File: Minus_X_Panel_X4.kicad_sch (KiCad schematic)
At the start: 9 parts

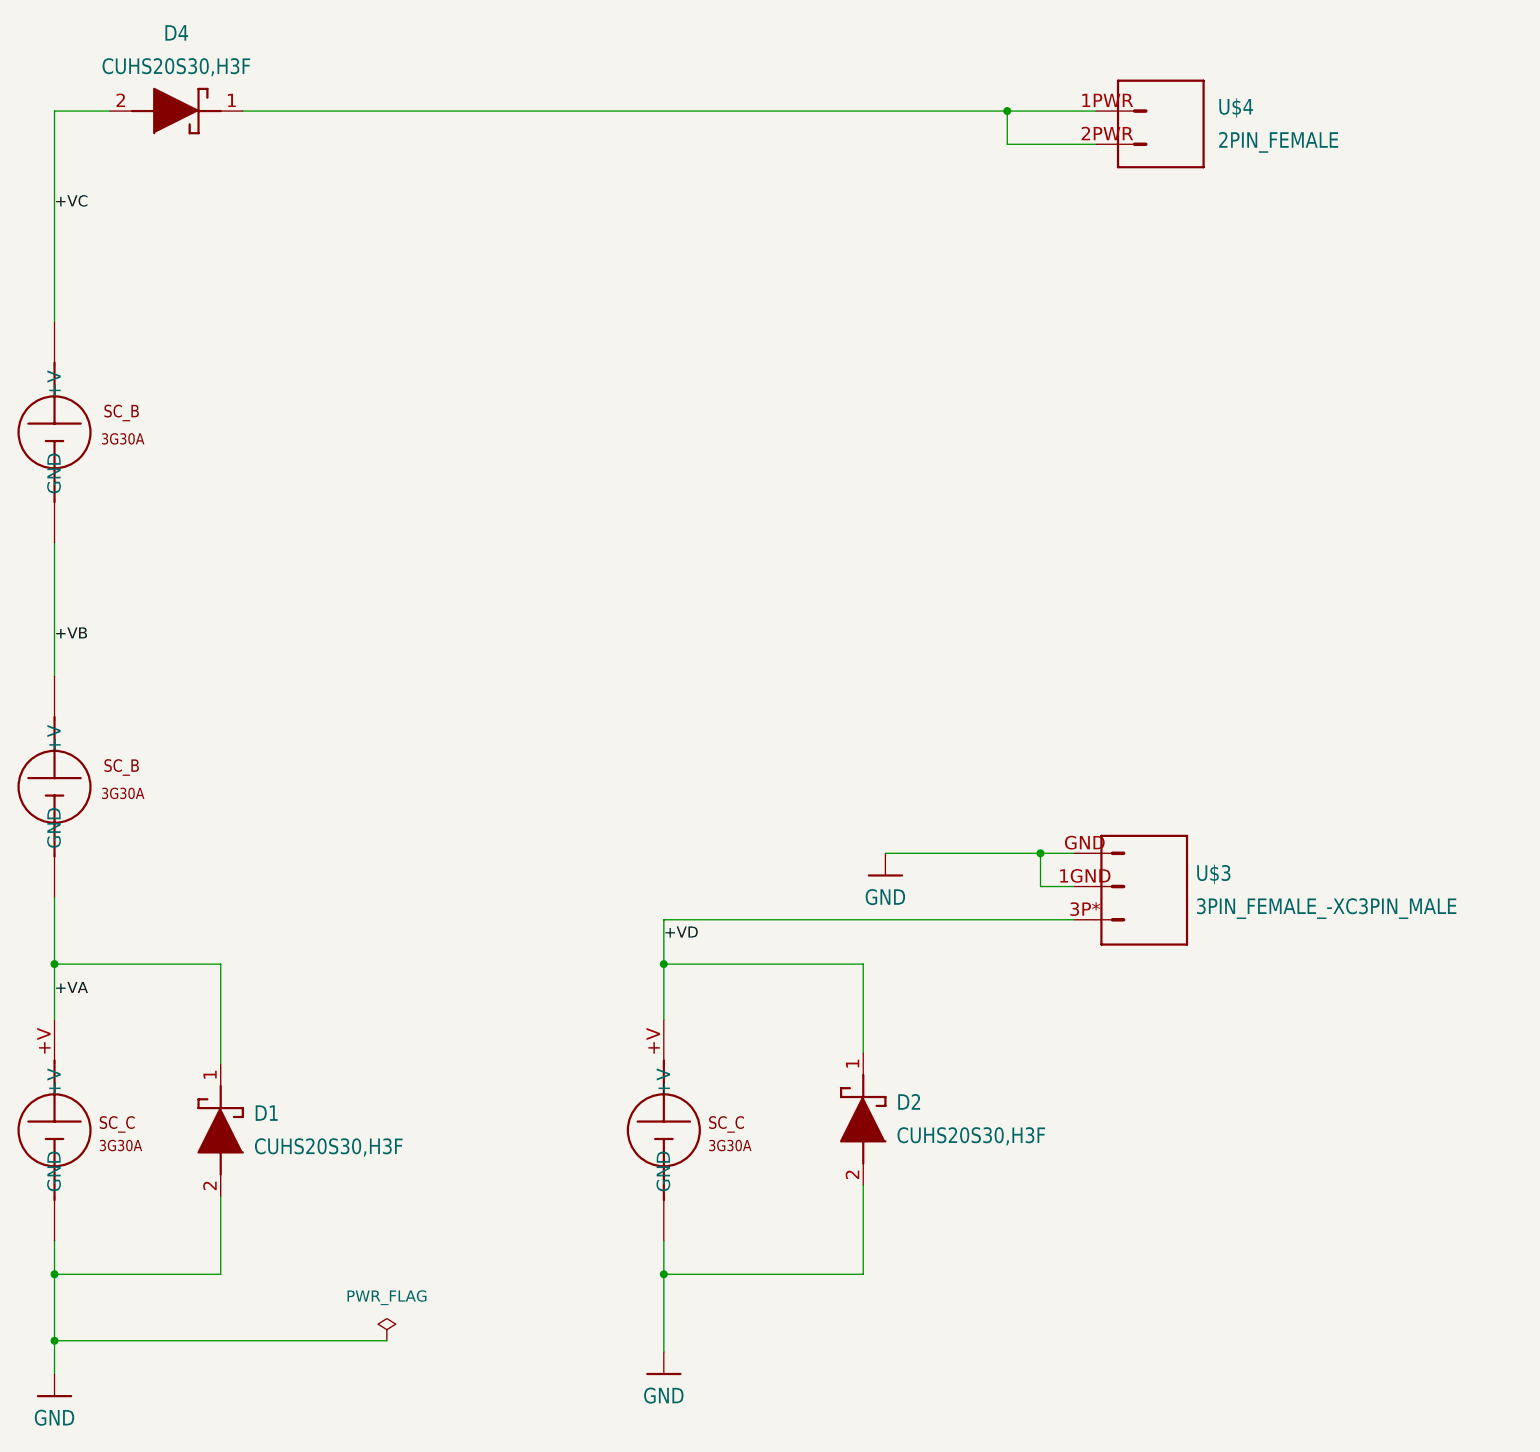
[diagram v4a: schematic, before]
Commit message: footprint of the Panel is modified with tracking
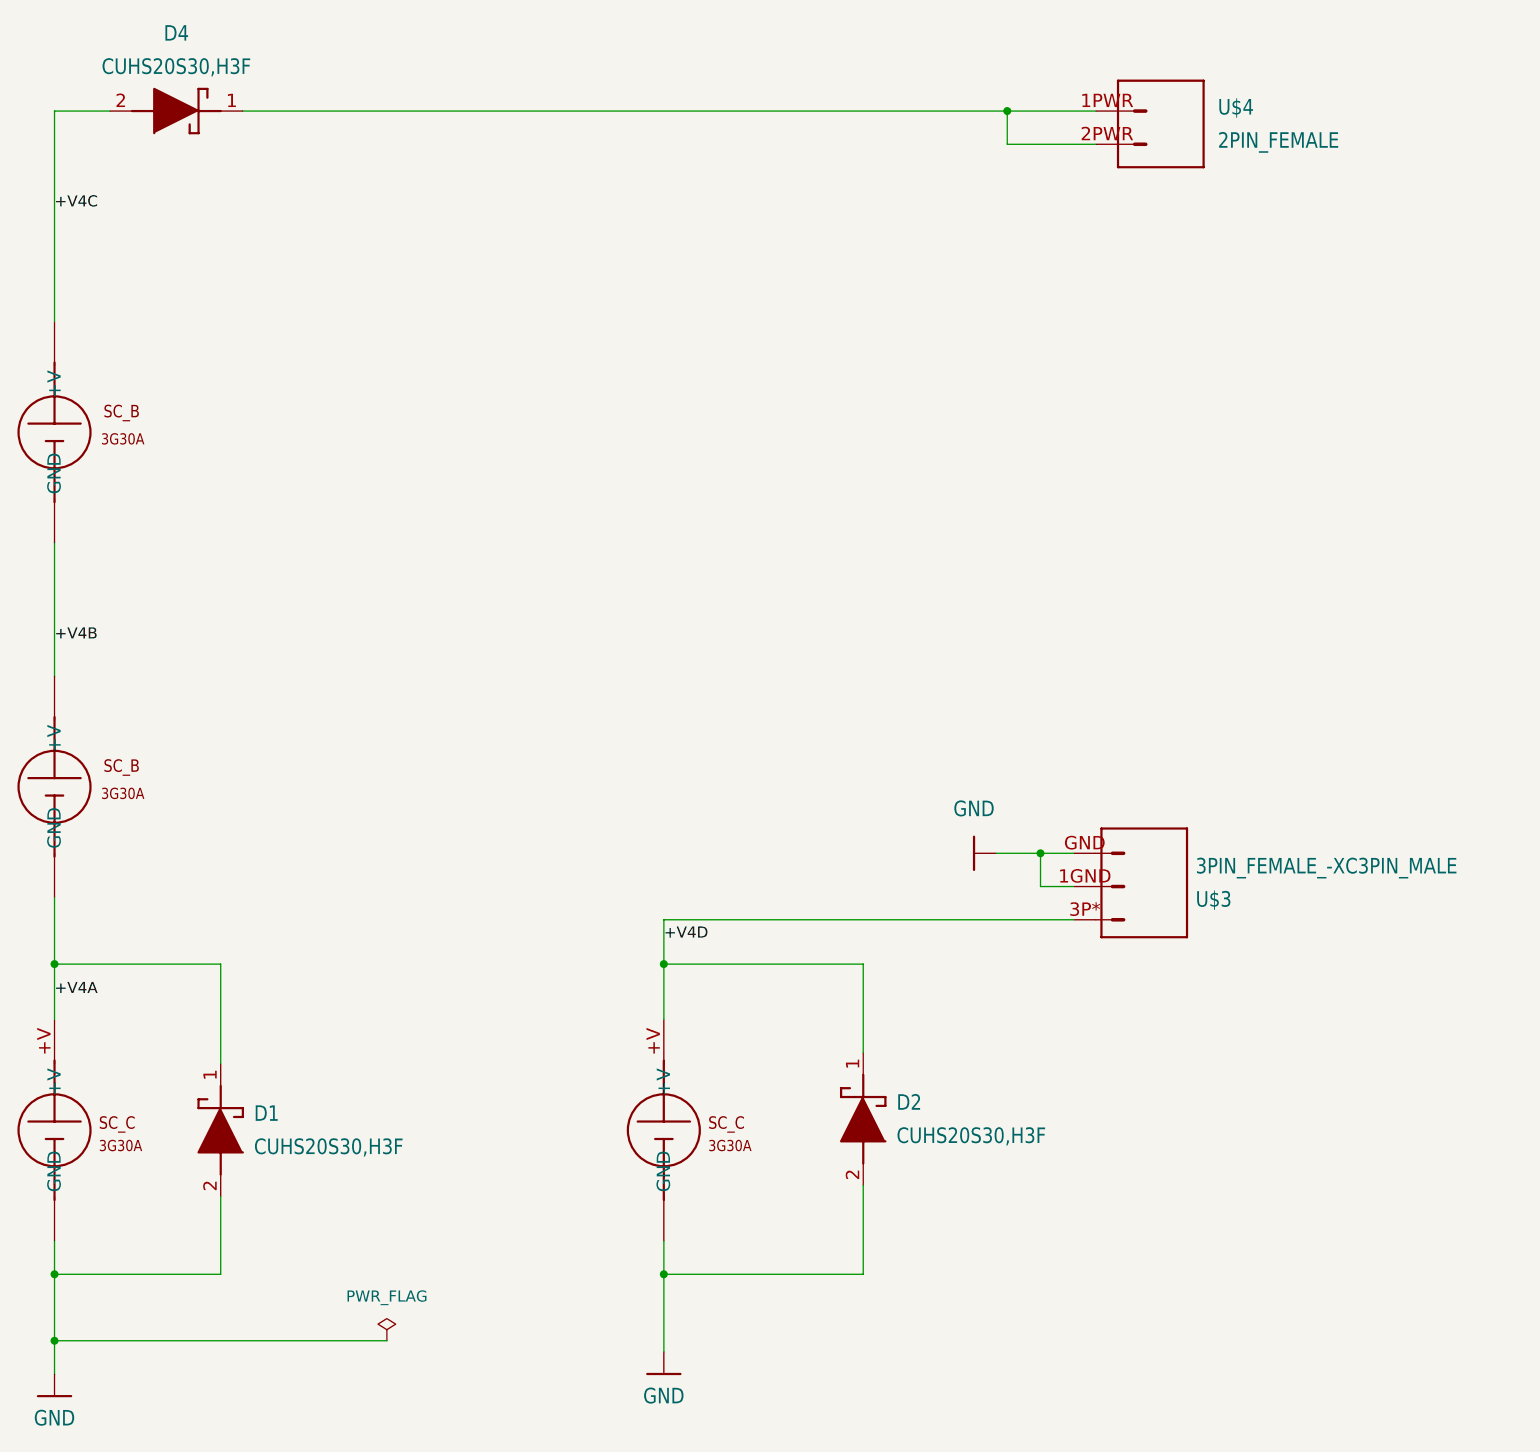
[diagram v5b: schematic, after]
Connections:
- net +VA renamed +V4A
- net +VB renamed +V4B
- net +VC renamed +V4C
- net +VD renamed +V4D
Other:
- moved on the sheet: U$3
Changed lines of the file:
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@@
 	(wire
 		(pts
-			(xy 133.35 127) (xy 151.13 127)
+			(xy 146.05 127) (xy 151.13 127)
 		)
 		(stroke
@@
 		)
 	)
-	(label "+VC"
+	(label "+V4C"
 		(at 38.1 53.34 0)
 		(effects
@@
 		)
 	)
-	(label "+VB"
+	(label "+V4B"
 		(at 38.1 102.87 0)
 		(effects
@@
 		)
 	)
-	(label "+VA"
+	(label "+V4A"
 		(at 38.1 143.51 0)
 		(effects
@@
 		)
 	)
-	(label "+VD"
+	(label "+V4D"
 		(at 107.95 137.16 0)
 		(effects
@@
 		(lib_id "Custom-Symbols:3PIN_FEMALE_-XC3PIN_MALE")
 		(at 160.02 130.81 0)
-		(unit 1)
-		(exclude_from_sim no)
-		(in_bom yes)
-		(on_board yes)
-		(dnp no)
-		(fields_autoplaced yes)
+		(mirror x)
+		(unit 1)
+		(exclude_from_sim no)
+		(in_bom yes)
+		(on_board yes)
+		(dnp no)
 		(property "Reference" "U$3"
-			(at 168.91 129.325 0)
+			(at 168.91 132.295 0)
 			(effects
 				(font
@@
 		)
 		(property "Value" "3PIN_FEMALE_-XC3PIN_MALE"
-			(at 168.91 133.135 0)
+			(at 168.91 128.485 0)
 			(effects
 				(font
@@
 	(symbol
 		(lib_id "Custom-Symbols:GND")
-		(at 133.35 129.54 0)
+		(at 143.51 127 270)
 		(unit 1)
 		(exclude_from_sim no)
@@
 		(fields_autoplaced yes)
 		(property "Reference" "#GND03"
-			(at 133.35 132.08 0)
+			(at 140.97 127 0)
 			(effects
 				(font
@@
 		)
 		(property "Value" "GND"
-			(at 133.35 132.08 0)
+			(at 143.51 121.92 90)
 			(effects
 				(font
@@
 		)
 		(property "Footprint" ""
-			(at 133.35 129.54 0)
+			(at 143.51 127 0)
 			(effects
 				(font
@@
 		)
 		(property "Datasheet" ""
-			(at 133.35 129.54 0)
+			(at 143.51 127 0)
 			(effects
 				(font
@@
 		)
 		(property "Description" ""
-			(at 133.35 129.54 0)
-			(effects
-				(font
+			(at 143.51 127 0)
+			(effects
+				(font
